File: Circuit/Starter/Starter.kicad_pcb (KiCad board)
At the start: 2 copper layers, 215.9 x 132.1 mm, 18 parts, among them J1 From Power, J2 Output+, J3 Output-, T1 BSH12-N406L 8:6400, T2 20:20, T3 20:20

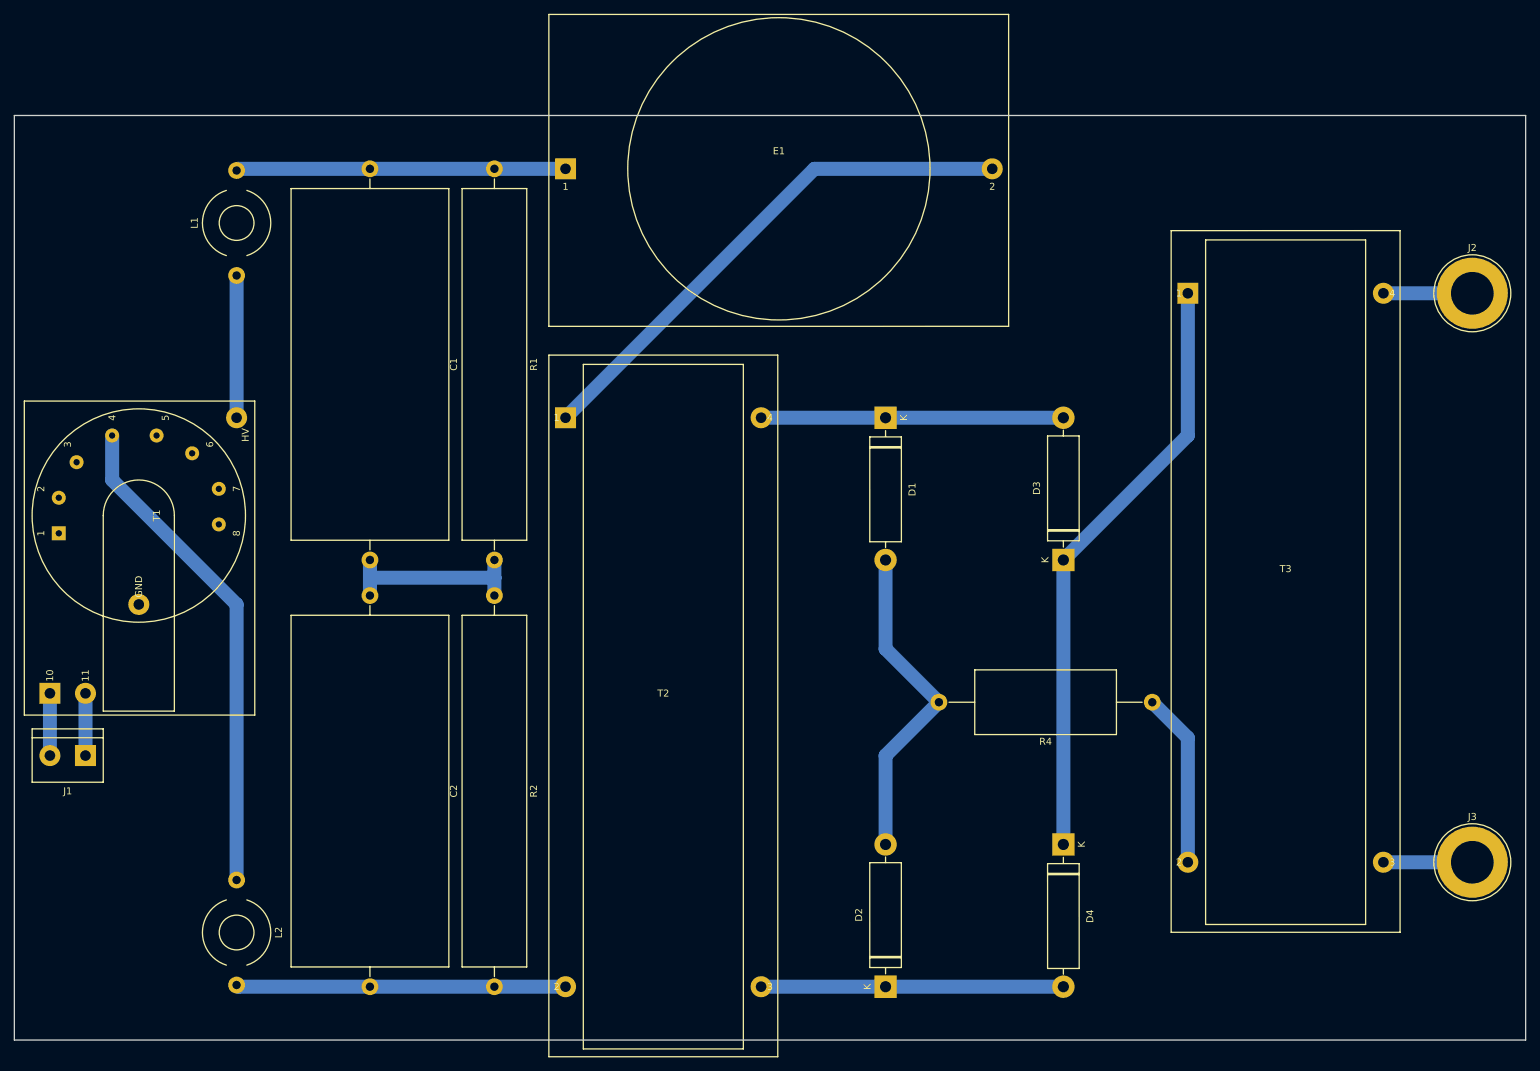
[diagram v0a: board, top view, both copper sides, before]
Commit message: [Circuit] Add screw holes to PCBs
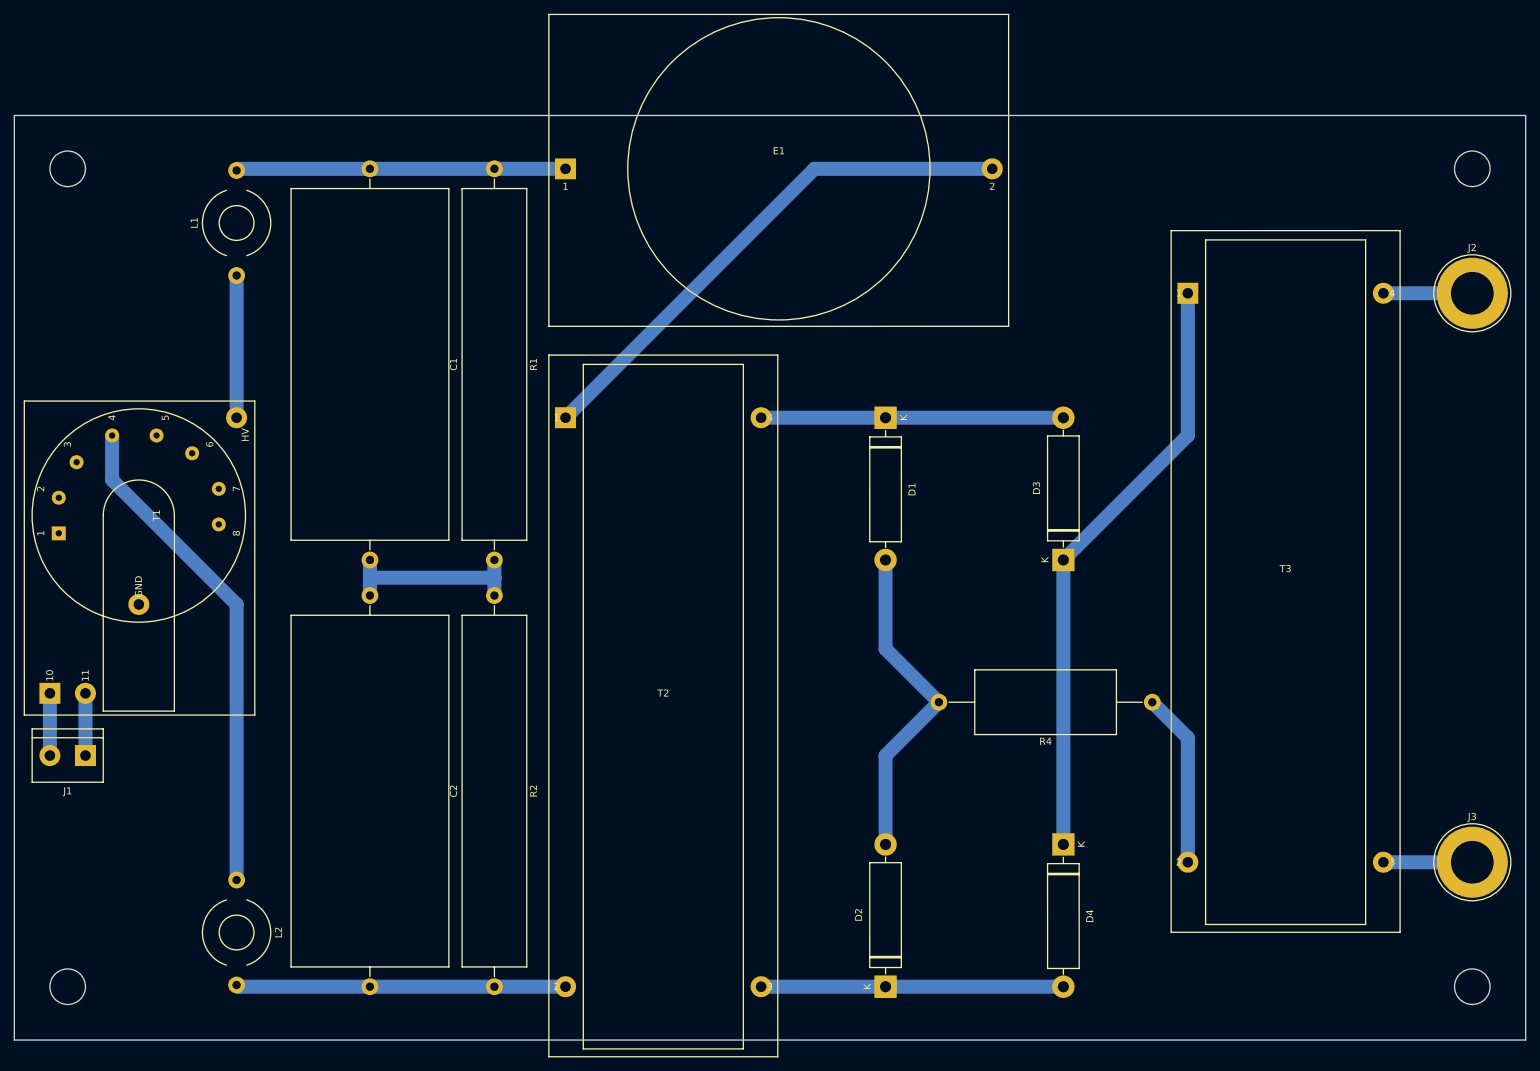
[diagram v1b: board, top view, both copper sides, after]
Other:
- outline, holes or cut-outs redrawn
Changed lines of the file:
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@@
   (general
     (thickness 1.6)
-    (drawings 4)
+    (drawings 8)
     (tracks 36)
     (zones 0)
@@
   )
   (setup
-    (last_trace_width 2)
+    (last_trace_width 0.25)
     (user_trace_width 0.5)
     (user_trace_width 2)
@@
     )
   )
+  (gr_circle (center 248.92 154.94) (end 251.46 154.94) (layer Edge.Cuts) (width 0.1))
+  (gr_circle (center 48.26 154.94) (end 45.72 154.94) (layer Edge.Cuts) (width 0.1))
+  (gr_circle (center 248.92 38.1) (end 251.46 38.1) (layer Edge.Cuts) (width 0.1))
+  (gr_circle (center 48.26 38.1) (end 50.8 38.1) (layer Edge.Cuts) (width 0.1))
   (gr_line (start 40.64 30.48) (end 40.64 162.56) (layer Edge.Cuts) (width 0.1))
   (gr_line (start 256.54 30.48) (end 40.64 30.48) (layer Edge.Cuts) (width 0.1))

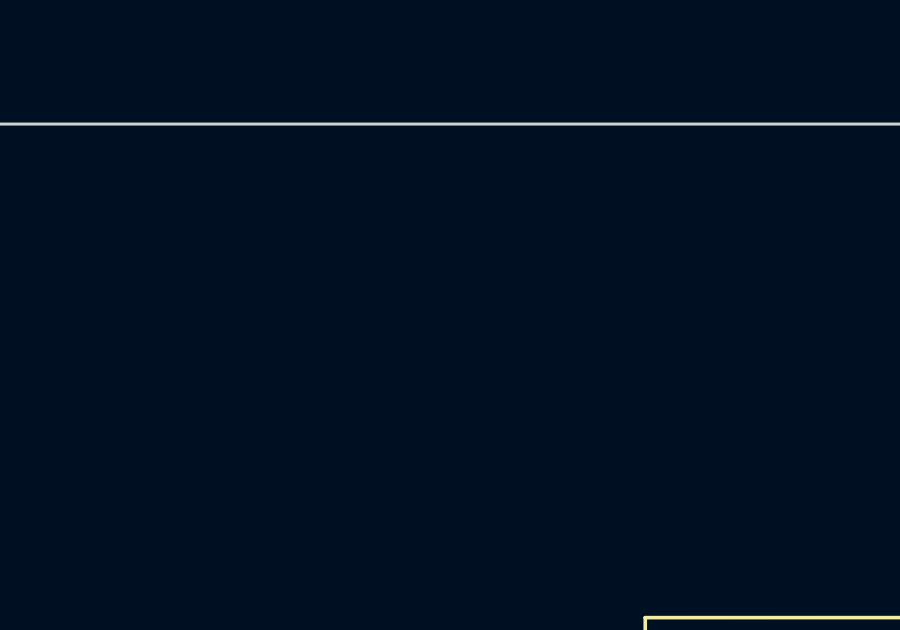
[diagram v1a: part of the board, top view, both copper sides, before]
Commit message: [Circuit] Enable to export gerber files
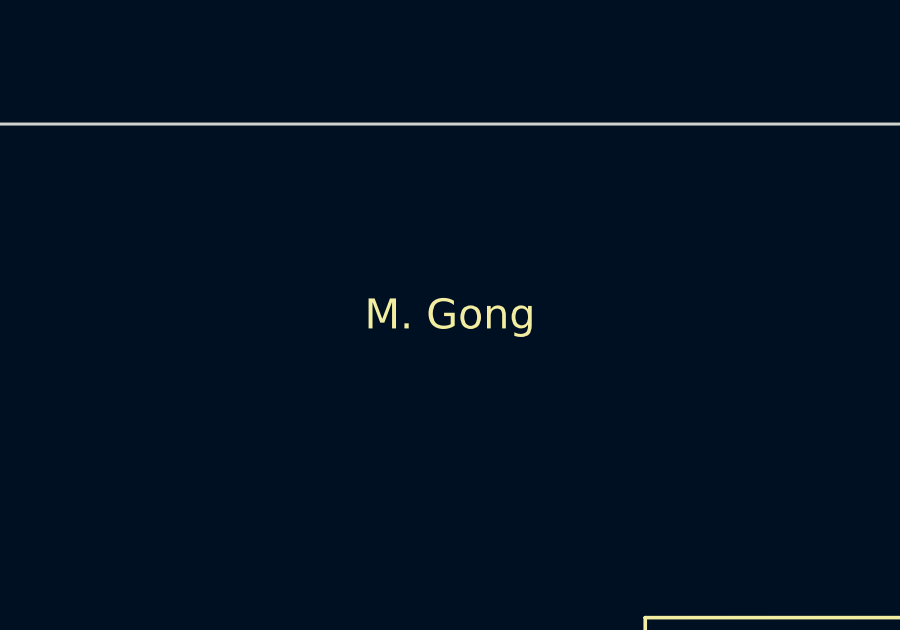
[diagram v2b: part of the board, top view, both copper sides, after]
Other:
- board text added: "M. Gong"
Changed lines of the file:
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@@
   (general
     (thickness 1.6)
-    (drawings 8)
+    (drawings 9)
     (tracks 36)
     (zones 0)
@@
       (creategerberjobfile false)
       (excludeedgelayer false)
-      (linewidth 0.100000)
+      (linewidth 0.250000)
       (plotframeref false)
       (viasonmask false)
@@
     )
   )
+  (gr_text "M. Gong" (at 199.39 36.83) (layer F.SilkS)
+    (effects (font (size 1 1) (thickness 0.15)))
+  )
   (gr_circle (center 248.92 154.94) (end 251.46 154.94) (layer Edge.Cuts) (width 0.1))

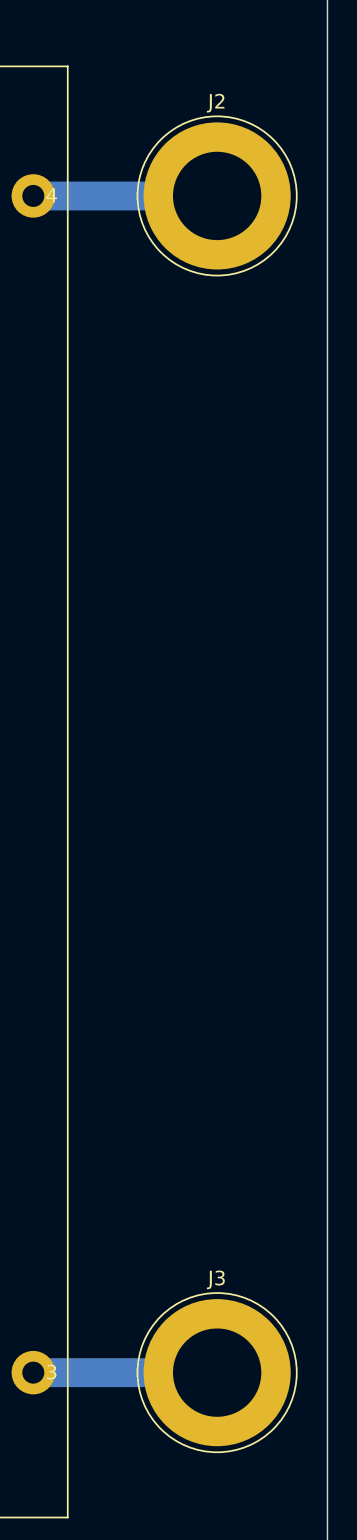
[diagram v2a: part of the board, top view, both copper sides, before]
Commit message: [Circuit] Use M6 bolt as the connectors of capacitor bank and starter
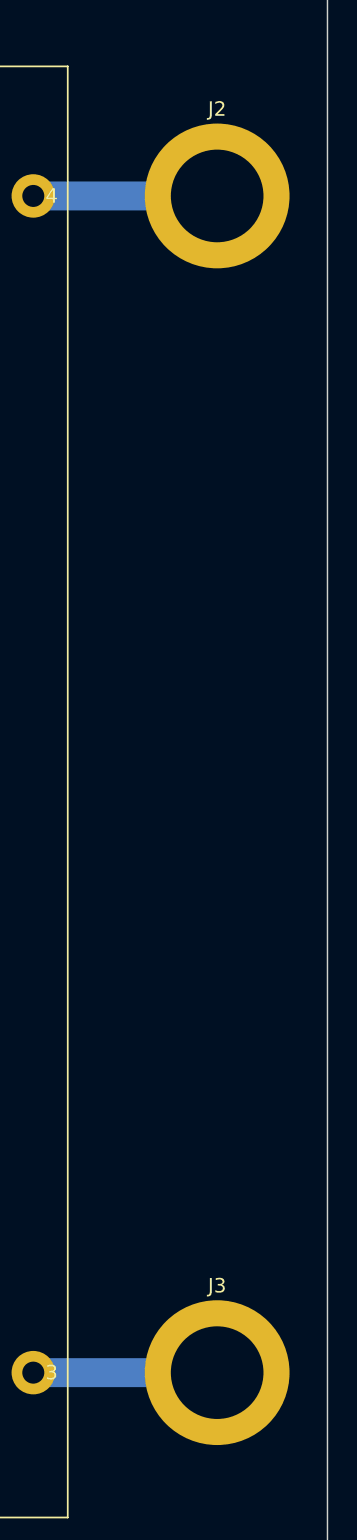
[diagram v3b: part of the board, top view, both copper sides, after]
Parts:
- J2, J3: footprint Connector:Banana_Jack_1Pin -> MountingHole:MountingHole_6.4mm_M6_ISO14580_Pad
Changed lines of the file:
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@@
     (add_net "Net-(R4-Pad1)")
+  )
+  (module MountingHole:MountingHole_6.4mm_M6_ISO14580_Pad (layer F.Cu)
+    (at 248.92 137.16)
+    (descr "Mounting Hole 6.4mm, M6, ISO14580")
+    (tags "mounting hole 6.4mm m6 iso14580")
+    (attr virtual)
+    (fp_text reference J3 (at 0 -6) (layer F.SilkS)
+      (effects (font (size 1 1) (thickness 0.15)))
+    )
+    (fp_text value Output- (at 0 6) (layer F.Fab)
+      (effects (font (size 1 1) (thickness 0.15)))
+    )
+    (fp_circle (center 0 0) (end 5.25 0) (layer F.CrtYd) (width 0.05))
+    (fp_circle (center 0 0) (end 5 0) (layer Cmts.User) (width 0.15))
+    (fp_text user %R (at 0.3 0) (layer F.Fab)
+      (effects (font (size 1 1) (thickness 0.15)))
+    )
+    (pad 1 thru_hole circle (at 0 0) (size 10 10) (drill 6.4) (layers *.Cu *.Mask)
+      (net 10 /Output-))
+  )
+  (module MountingHole:MountingHole_6.4mm_M6_ISO14580_Pad (layer F.Cu)
+    (at 248.92 55.88)
+    (descr "Mounting Hole 6.4mm, M6, ISO14580")
+    (tags "mounting hole 6.4mm m6 iso14580")
+    (attr virtual)
+    (fp_text reference J2 (at 0 -6) (layer F.SilkS)
+      (effects (font (size 1 1) (thickness 0.15)))
+    )
+    (fp_text value Output+ (at 0 6) (layer F.Fab)
+      (effects (font (size 1 1) (thickness 0.15)))
+    )
+    (fp_circle (center 0 0) (end 5.25 0) (layer F.CrtYd) (width 0.05))
+    (fp_circle (center 0 0) (end 5 0) (layer Cmts.User) (width 0.15))
+    (fp_text user %R (at 0.3 0) (layer F.Fab)
+      (effects (font (size 1 1) (thickness 0.15)))
+    )
+    (pad 1 thru_hole circle (at 0 0) (size 10 10) (drill 6.4) (layers *.Cu *.Mask)
+      (net 9 /Output+))
   )
   (module Resistor_THT:R_Axial_DIN0922_L20.0mm_D9.0mm_P30.48mm_Horizontal (layer F.Cu)
@@
     )
   )
-  (module Connector:Banana_Jack_1Pin (layer F.Cu)
-    (at 248.92 55.88)
-    (descr "Single banana socket, footprint - 6mm drill")
-    (tags "banana socket")
-    (fp_text reference J2 (at 0 -6.5) (layer F.SilkS)
-      (effects (font (size 1 1) (thickness 0.15)))
-    )
-    (fp_text value Output+ (at -0.25 6.5) (layer F.Fab)
-      (effects (font (size 1 1) (thickness 0.15)))
-    )
-    (fp_text user %R (at 0 0) (layer F.Fab)
-      (effects (font (size 0.8 0.8) (thickness 0.12)))
-    )
-    (fp_circle (center 0 0) (end 5.75 0) (layer F.CrtYd) (width 0.05))
-    (fp_circle (center 0 0) (end 2 0) (layer F.Fab) (width 0.1))
-    (fp_circle (center 0 0) (end 4.85 0.05) (layer F.Fab) (width 0.1))
-    (fp_circle (center 0 0) (end 5.5 0) (layer F.SilkS) (width 0.12))
-    (pad 1 thru_hole circle (at 0 0) (size 10.16 10.16) (drill 6.1) (layers *.Cu *.Mask)
-      (net 9 /Output+))
-    (model ${KISYS3DMOD}/Connector.3dshapes/Banana_Jack_1Pin.wrl
-      (at (xyz 0 0 0))
-      (scale (xyz 2 2 2))
-      (rotate (xyz 0 0 0))
-    )
-  )
   (module Inductor_THT:L_Toroid_Horizontal_D9.5mm_P15.00mm_Diameter10-5mm_Amidon-T37 (layer F.Cu)
     (at 72.39 139.7 270)
@@
       (rotate (xyz 0 0 0))
     )
-  )
-  (module Connector:Banana_Jack_1Pin (layer F.Cu)
-    (at 248.92 137.16)
-    (descr "Single banana socket, footprint - 6mm drill")
-    (tags "banana socket")
-    (fp_text reference J3 (at 0 -6.5) (layer F.SilkS)
-      (effects (font (size 1 1) (thickness 0.15)))
-    )
-    (fp_text value Output- (at -0.25 6.5) (layer F.Fab)
-      (effects (font (size 1 1) (thickness 0.15)))
-    )
-    (fp_text user %R (at 0 0) (layer F.Fab)
-      (effects (font (size 0.8 0.8) (thickness 0.12)))
-    )
-    (fp_circle (center 0 0) (end 5.75 0) (layer F.CrtYd) (width 0.05))
-    (fp_circle (center 0 0) (end 2 0) (layer F.Fab) (width 0.1))
-    (fp_circle (center 0 0) (end 4.85 0.05) (layer F.Fab) (width 0.1))
-    (fp_circle (center 0 0) (end 5.5 0) (layer F.SilkS) (width 0.12))
-    (pad 1 thru_hole circle (at 0 0) (size 10.16 10.16) (drill 6.1) (layers *.Cu *.Mask)
-      (net 10 /Output-))
-    (model ${KISYS3DMOD}/Connector.3dshapes/Banana_Jack_1Pin.wrl
-      (at (xyz 0 0 0))
-      (scale (xyz 2 2 2))
-      (rotate (xyz 0 0 0))
-    )
